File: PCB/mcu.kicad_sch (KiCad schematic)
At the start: 39 parts, among them J101 switch, J102 switch, J103 USB4510-03-1-A, J104 CONN_DISPLAY, U101 W25Q128JVSIQ, U102 RP2040, U103 TPS62172DSG, U104 USBLC6-2SC6, Y101 12MHz

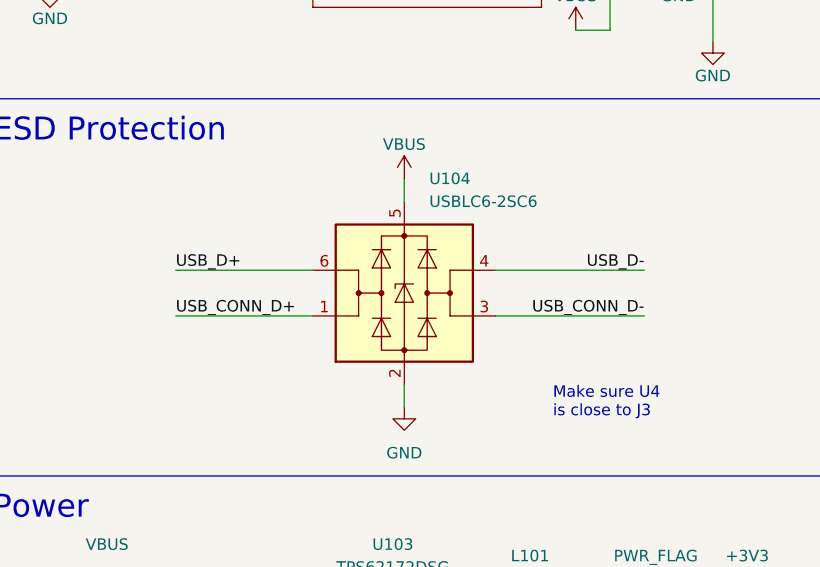
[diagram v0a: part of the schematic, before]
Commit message: Swap usb pair
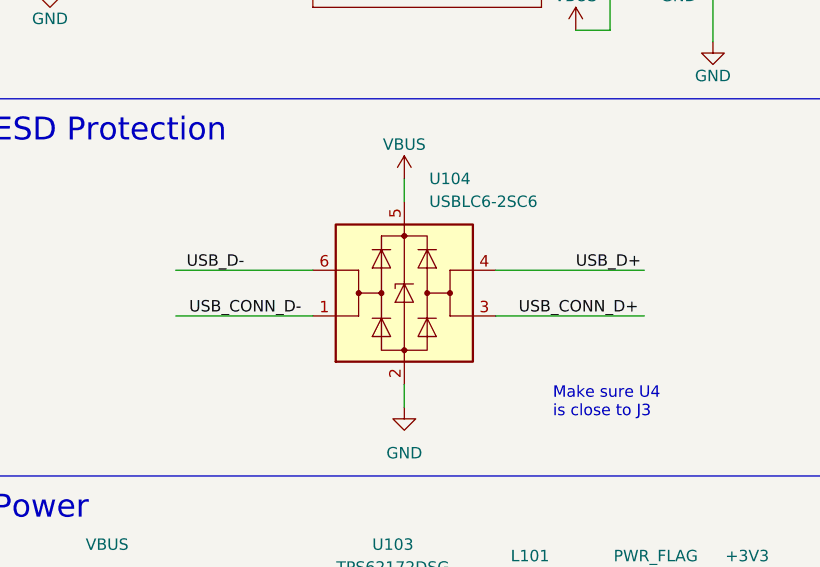
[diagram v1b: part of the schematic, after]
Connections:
- net USB_CONN_D+: now also U104.3 (I/O2); no longer U104.1 (I/O1)
- net USB_CONN_D-: now also U104.1 (I/O1); no longer U104.3 (I/O2)
- net USB_D+: now also U104.4 (I/O2); no longer U104.6 (I/O1)
- net USB_D-: now also U104.6 (I/O1); no longer U104.4 (I/O2)
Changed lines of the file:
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@@
     (effects (font (size 1.27 1.27)) (justify left bottom))
+  )
+  (label "USB_D-" (at 218.44 78.74 180)
+    (effects (font (size 1.27 1.27)) (justify right bottom))
+  )
+  (label "USB_CONN_D-" (at 224.79 83.82 180)
+    (effects (font (size 1.27 1.27)) (justify right bottom))
   )
   (label "~{BOOTSEL}" (at 34.29 38.1 0)
@@
     (effects (font (size 1.27 1.27)) (justify left bottom))
   )
-  (label "XIN" (at 76.2 97.79 0)
+  (label "USB_D+" (at 255.27 78.74 0)
     (effects (font (size 1.27 1.27)) (justify left bottom))
   )
-  (label "USB_CONN_D+" (at 210.82 83.82 0)
+  (label "XIN" (at 76.2 97.79 0)
     (effects (font (size 1.27 1.27)) (justify left bottom))
   )
@@
     (effects (font (size 1.27 1.27)) (justify left bottom))
   )
-  (label "USB_D-" (at 262.89 78.74 180)
+  (label "QSPI_SD0" (at 62.23 72.39 180)
     (effects (font (size 1.27 1.27)) (justify right bottom))
   )
-  (label "QSPI_SD0" (at 62.23 72.39 180)
-    (effects (font (size 1.27 1.27)) (justify right bottom))
+  (label "USB_CONN_D+" (at 248.92 83.82 0)
+    (effects (font (size 1.27 1.27)) (justify left bottom))
   )
   (label "QSPI_SD3" (at 76.2 74.93 0)
@@
   (label "XOUT" (at 50.8 113.03 0)
     (effects (font (size 1.27 1.27)) (justify left bottom))
-  )
-  (label "USB_CONN_D-" (at 262.89 83.82 180)
-    (effects (font (size 1.27 1.27)) (justify right bottom))
   )
   (label "SCL" (at 162.56 100.33 180)
@@
     (effects (font (size 1.27 1.27)) (justify left bottom))
   )
-  (label "USB_D+" (at 210.82 78.74 0)
-    (effects (font (size 1.27 1.27)) (justify left bottom))
-  )

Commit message: less crude outline
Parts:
- J104: footprint (none) -> Footprints:OLED_128_64
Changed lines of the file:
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@@
       (effects (font (size 1.27 1.27)) (justify right))
     )
-    (property "Footprint" "" (id 2) (at 257.81 157.48 0)
+    (property "Footprint" "Footprints:OLED_128_64" (id 2) (at 257.81 157.48 0)
       (effects (font (size 1.27 1.27)) hide)
     )

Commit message: Work
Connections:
- net ROW-1: now also U102.32 (GPIO21); no longer U102.4 (GPIO2)
- net ROW-2: now also U102.31 (GPIO20); no longer U102.5 (GPIO3)
- net ROW-3: now also U102.30 (GPIO19); no longer U102.6 (GPIO4)
- net ROW-4: now reaches U102.29 (GPIO18)
- net COL-6: no longer names the net of U102.13 (GPIO10)
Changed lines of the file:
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@@
   (junction (at 102.87 39.37) (diameter 0) (color 0 0 0 0)
   )
+  (no_connect (at 156.21 72.39))
   (no_connect (at 83.82 129.54))
   (no_connect (at 156.21 138.43))
@@
   (no_connect (at 156.21 105.41))
   (no_connect (at 156.21 95.25))
-  (no_connect (at 156.21 110.49))
-  (no_connect (at 156.21 113.03))
-  (no_connect (at 156.21 107.95))
+  (no_connect (at 156.21 87.63))
   (no_connect (at 156.21 123.19))
   (no_connect (at 156.21 92.71))
-  (no_connect (at 156.21 115.57))
   (no_connect (at 156.21 135.89))
   (no_connect (at 156.21 90.17))
   (no_connect (at 156.21 130.81))
   (no_connect (at 83.82 127))
+  (no_connect (at 156.21 69.85))
+  (no_connect (at 156.21 67.31))
   (no_connect (at 259.08 31.75))
   (no_connect (at 156.21 120.65))
@@
     (stroke (width 0) (type default) (color 0 0 0 0))
   )
-  (wire (pts (xy 158.75 72.39) (xy 152.4 72.39))
-    (stroke (width 0) (type default) (color 0 0 0 0))
-  )
   (wire (pts (xy 259.08 39.37) (xy 270.51 39.37))
     (stroke (width 0) (type default) (color 0 0 0 0))
@@
     (stroke (width 0) (type default) (color 0 0 0 0))
   )
-  (wire (pts (xy 156.21 115.57) (xy 152.4 115.57))
+  (wire (pts (xy 152.4 115.57) (xy 158.75 115.57))
     (stroke (width 0) (type default) (color 0 0 0 0))
   )
@@
     (stroke (width 0) (type default) (color 0 0 0 0))
   )
-  (wire (pts (xy 156.21 110.49) (xy 152.4 110.49))
+  (wire (pts (xy 152.4 110.49) (xy 158.75 110.49))
     (stroke (width 0) (type default) (color 0 0 0 0))
   )
@@
     (stroke (width 0) (type default) (color 0 0 0 0))
   )
+  (wire (pts (xy 152.4 87.63) (xy 156.21 87.63))
+    (stroke (width 0) (type default) (color 0 0 0 0))
+  )
   (wire (pts (xy 156.21 123.19) (xy 152.4 123.19))
     (stroke (width 0) (type default) (color 0 0 0 0))
@@
     (stroke (width 0) (type default) (color 0 0 0 0))
   )
-  (wire (pts (xy 158.75 87.63) (xy 152.4 87.63))
-    (stroke (width 0) (type default) (color 0 0 0 0))
-  )
   (wire (pts (xy 27.94 191.77) (xy 25.4 191.77))
     (stroke (width 0) (type default) (color 0 0 0 0))
@@
     (stroke (width 0) (type default) (color 0 0 0 0))
   )
-  (wire (pts (xy 156.21 107.95) (xy 152.4 107.95))
+  (wire (pts (xy 152.4 107.95) (xy 158.75 107.95))
     (stroke (width 0) (type default) (color 0 0 0 0))
   )
@@
     (stroke (width 0) (type default) (color 0 0 0 0))
   )
-  (wire (pts (xy 158.75 69.85) (xy 152.4 69.85))
-    (stroke (width 0) (type default) (color 0 0 0 0))
-  )
   (wire (pts (xy 157.48 52.07) (xy 157.48 49.53))
     (stroke (width 0) (type default) (color 0 0 0 0))
@@
     (stroke (width 0) (type default) (color 0 0 0 0))
   )
+  (wire (pts (xy 152.4 72.39) (xy 156.21 72.39))
+    (stroke (width 0) (type default) (color 0 0 0 0))
+  )
   (wire (pts (xy 166.37 187.96) (xy 166.37 189.23))
     (stroke (width 0) (type default) (color 0 0 0 0))
@@
     (stroke (width 0) (type default) (color 0 0 0 0))
   )
-  (wire (pts (xy 158.75 67.31) (xy 152.4 67.31))
-    (stroke (width 0) (type default) (color 0 0 0 0))
-  )
   (wire (pts (xy 217.17 161.29) (xy 233.68 161.29))
     (stroke (width 0) (type default) (color 0 0 0 0))
@@
     (stroke (width 0) (type default) (color 0 0 0 0))
   )
+  (wire (pts (xy 152.4 69.85) (xy 156.21 69.85))
+    (stroke (width 0) (type default) (color 0 0 0 0))
+  )
   (wire (pts (xy 262.89 83.82) (xy 246.38 83.82))
     (stroke (width 0) (type default) (color 0 0 0 0))
@@
     (stroke (width 0) (type default) (color 0 0 0 0))
   )
+  (wire (pts (xy 152.4 67.31) (xy 156.21 67.31))
+    (stroke (width 0) (type default) (color 0 0 0 0))
+  )
   (wire (pts (xy 88.9 78.74) (xy 76.2 78.74))
     (stroke (width 0) (type default) (color 0 0 0 0))
@@
     (stroke (width 0) (type default) (color 0 0 0 0))
   )
-  (wire (pts (xy 156.21 113.03) (xy 152.4 113.03))
+  (wire (pts (xy 152.4 113.03) (xy 158.75 113.03))
     (stroke (width 0) (type default) (color 0 0 0 0))
   )
@@
     (effects (font (size 1.27 1.27)) (justify left bottom))
   )
-  (hierarchical_label "ROW-2" (shape input) (at 158.75 69.85 0)
-    (effects (font (size 1.27 1.27)) (justify left))
-  )
   (hierarchical_label "COL-1" (shape input) (at 158.75 74.93 0)
     (effects (font (size 1.27 1.27)) (justify left))
   )
+  (hierarchical_label "ROW-3" (shape input) (at 158.75 110.49 0)
+    (effects (font (size 1.27 1.27)) (justify left))
+  )
   (hierarchical_label "COL-2" (shape input) (at 158.75 77.47 0)
     (effects (font (size 1.27 1.27)) (justify left))
   )
+  (hierarchical_label "ROW-4" (shape input) (at 158.75 107.95 0)
+    (effects (font (size 1.27 1.27)) (justify left))
+  )
   (hierarchical_label "COL-4" (shape input) (at 158.75 82.55 0)
     (effects (font (size 1.27 1.27)) (justify left))
   )
-  (hierarchical_label "ROW-1" (shape input) (at 158.75 67.31 0)
-    (effects (font (size 1.27 1.27)) (justify left))
-  )
-  (hierarchical_label "ROW-3" (shape input) (at 158.75 72.39 0)
-    (effects (font (size 1.27 1.27)) (justify left))
-  )
   (hierarchical_label "COL-5" (shape input) (at 158.75 85.09 0)
     (effects (font (size 1.27 1.27)) (justify left))
@@
     (effects (font (size 1.27 1.27)) (justify left))
   )
-  (hierarchical_label "COL-6" (shape input) (at 158.75 87.63 0)
-    (effects (font (size 1.27 1.27)) (justify left))
-  )
   (hierarchical_label "TX" (shape input) (at 158.75 62.23 0)
     (effects (font (size 1.27 1.27)) (justify left))
@@
     (effects (font (size 1.27 1.27)) (justify left))
   )
+  (hierarchical_label "ROW-1" (shape input) (at 158.75 115.57 0)
+    (effects (font (size 1.27 1.27)) (justify left))
+  )
+  (hierarchical_label "ROW-2" (shape input) (at 158.75 113.03 0)
+    (effects (font (size 1.27 1.27)) (justify left))
+  )

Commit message: Metric
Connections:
- net +3.3V is gone; now on net +3V3: J104.2 (Pin_2), Y101.4
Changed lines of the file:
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@@
   (junction (at 129.54 189.23) (diameter 0) (color 0 0 0 0)
   )
-  (junction (at 245.11 161.29) (diameter 0) (color 0 0 0 0)
-  )
   (junction (at 39.37 60.96) (diameter 0) (color 0 0 0 0)
   )
@@
   )
   (junction (at 102.87 39.37) (diameter 0) (color 0 0 0 0)
+  )
+  (junction (at 243.84 160.02) (diameter 0) (color 0 0 0 0)
   )
   (no_connect (at 156.21 72.39))
@@
     (pin "2")
   )
+  (symbol (lib_id "power:+3V3") (at 243.84 160.02 0) (unit 1)
+    (in_bom yes) (on_board yes)
+    (property "Reference" "#PWR?" (id 0) (at 243.84 163.83 0)
+      (effects (font (size 1.27 1.27)) hide)
+    )
+    (property "Value" "+3V3" (id 1) (at 244.221 155.6258 0))
+    (property "Footprint" "" (id 2) (at 243.84 160.02 0)
+      (effects (font (size 1.27 1.27)) hide)
+    )
+    (property "Datasheet" "" (id 3) (at 243.84 160.02 0)
+      (effects (font (size 1.27 1.27)) hide)
+    )
+    (pin "1")
+  )
   (symbol (lib_id "Device:R") (at 49.53 38.1 270) (unit 1)
     (in_bom yes) (on_board yes)
@@
     (pin "1")
   )
-  (symbol (lib_id "power:+3.3V") (at 245.11 161.29 0) (unit 1)
-    (in_bom yes) (on_board yes)
-    (property "Reference" "#PWR0126" (id 0) (at 245.11 165.1 0)
-      (effects (font (size 1.27 1.27)) hide)
-    )
-    (property "Value" "+3.3V" (id 1) (at 245.11 157.48 0))
-    (property "Footprint" "" (id 2) (at 245.11 161.29 0)
-      (effects (font (size 1.27 1.27)) hide)
-    )
-    (property "Datasheet" "" (id 3) (at 245.11 161.29 0)
-      (effects (font (size 1.27 1.27)) hide)
-    )
-    (pin "1")
-  )
   (symbol (lib_id "Device:C") (at 49.53 60.96 90) (unit 1)
     (in_bom yes) (on_board yes)
@@
     (pin "1")
     (pin "2")
-  )
-  (symbol (lib_id "power:+3.3V") (at 45.72 137.16 0) (unit 1)
-    (in_bom yes) (on_board yes)
-    (property "Reference" "#PWR0109" (id 0) (at 45.72 140.97 0)
-      (effects (font (size 1.27 1.27)) hide)
-    )
-    (property "Value" "+3.3V" (id 1) (at 45.72 133.35 0))
-    (property "Footprint" "" (id 2) (at 45.72 137.16 0)
-      (effects (font (size 1.27 1.27)) hide)
-    )
-    (property "Datasheet" "" (id 3) (at 45.72 137.16 0)
-      (effects (font (size 1.27 1.27)) hide)
-    )
-    (pin "1")
   )
   (symbol (lib_id "power:+3V3") (at 49.53 176.53 0) (unit 1)
@@
     (pin "2")
   )
+  (symbol (lib_id "power:+3V3") (at 45.72 137.16 0) (unit 1)
+    (in_bom yes) (on_board yes)
+    (property "Reference" "#PWR0109" (id 0) (at 45.72 140.97 0)
+      (effects (font (size 1.27 1.27)) hide)
+    )
+    (property "Value" "+3V3" (id 1) (at 46.101 132.7658 0))
+    (property "Footprint" "" (id 2) (at 45.72 137.16 0)
+      (effects (font (size 1.27 1.27)) hide)
+    )
+    (property "Datasheet" "" (id 3) (at 45.72 137.16 0)
+      (effects (font (size 1.27 1.27)) hide)
+    )
+    (pin "1")
+  )
   (symbol (lib_id "power:GND") (at 196.85 46.99 0) (unit 1)

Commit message: Add switch footprint
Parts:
- J102: footprint Connector_PinHeader_2.54mm:PinHeader_1x02_P2.54mm_Vertical -> Footprints:SKHLACA010
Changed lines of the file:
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@@
   (symbol (lib_id "power:+3V3") (at 243.84 160.02 0) (unit 1)
     (in_bom yes) (on_board yes)
-    (property "Reference" "#PWR?" (id 0) (at 243.84 163.83 0)
+    (property "Reference" "#PWR0126" (id 0) (at 243.84 163.83 0)
       (effects (font (size 1.27 1.27)) hide)
     )
@@
     (property "Reference" "J102" (id 0) (at 26.67 34.29 0))
     (property "Value" "switch" (id 1) (at 27.94 40.64 0))
-    (property "Footprint" "Connector_PinHeader_2.54mm:PinHeader_1x02_P2.54mm_Vertical" (id 2) (at 27.94 33.02 0)
+    (property "Footprint" "Footprints:SKHLACA010" (id 2) (at 27.94 33.02 0)
       (effects (font (size 1.27 1.27)) hide)
     )

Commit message: add OLED footprint
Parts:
- J101: footprint Connector_PinHeader_2.54mm:PinHeader_1x02_P2.54mm_Vertical -> Footprints:SKHLACA010
- J104: footprint Footprints:OLED_128_64 -> Footprints:SSD1306_0.96_Oled
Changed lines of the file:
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@@
     (property "Reference" "J101" (id 0) (at 26.67 22.86 0))
     (property "Value" "switch" (id 1) (at 27.94 29.21 0))
-    (property "Footprint" "Connector_PinHeader_2.54mm:PinHeader_1x02_P2.54mm_Vertical" (id 2) (at 27.94 21.59 0)
+    (property "Footprint" "Footprints:SKHLACA010" (id 2) (at 27.94 21.59 0)
       (effects (font (size 1.27 1.27)) hide)
     )
@@
   )
   (symbol (lib_id "Connector:Conn_01x04_Male") (at 257.81 157.48 180) (unit 1)
-    (in_bom yes) (on_board yes) (fields_autoplaced)
-    (property "Reference" "J104" (id 0) (at 259.08 154.9399 0)
+    (in_bom yes) (on_board yes)
+    (property "Reference" "J104" (id 0) (at 259.08 154.94 0)
       (effects (font (size 1.27 1.27)) (justify right))
     )
@@
       (effects (font (size 1.27 1.27)) (justify right))
     )
-    (property "Footprint" "Footprints:OLED_128_64" (id 2) (at 257.81 157.48 0)
-      (effects (font (size 1.27 1.27)) hide)
-    )
+    (property "Footprint" "Footprints:SSD1306_0.96_Oled" (id 2) (at 257.81 157.48 0)
+      (effects (font (size 1.27 1.27)) hide)
+    )
